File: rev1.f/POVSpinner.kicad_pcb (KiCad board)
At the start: 2 copper layers, 25.3 x 76.4 mm, 26 parts, among them P1 ISP, SW1 SW_RESET, SW2 SW_POWER, U1 Microchip_ATtiny85, X1 USBMICRO

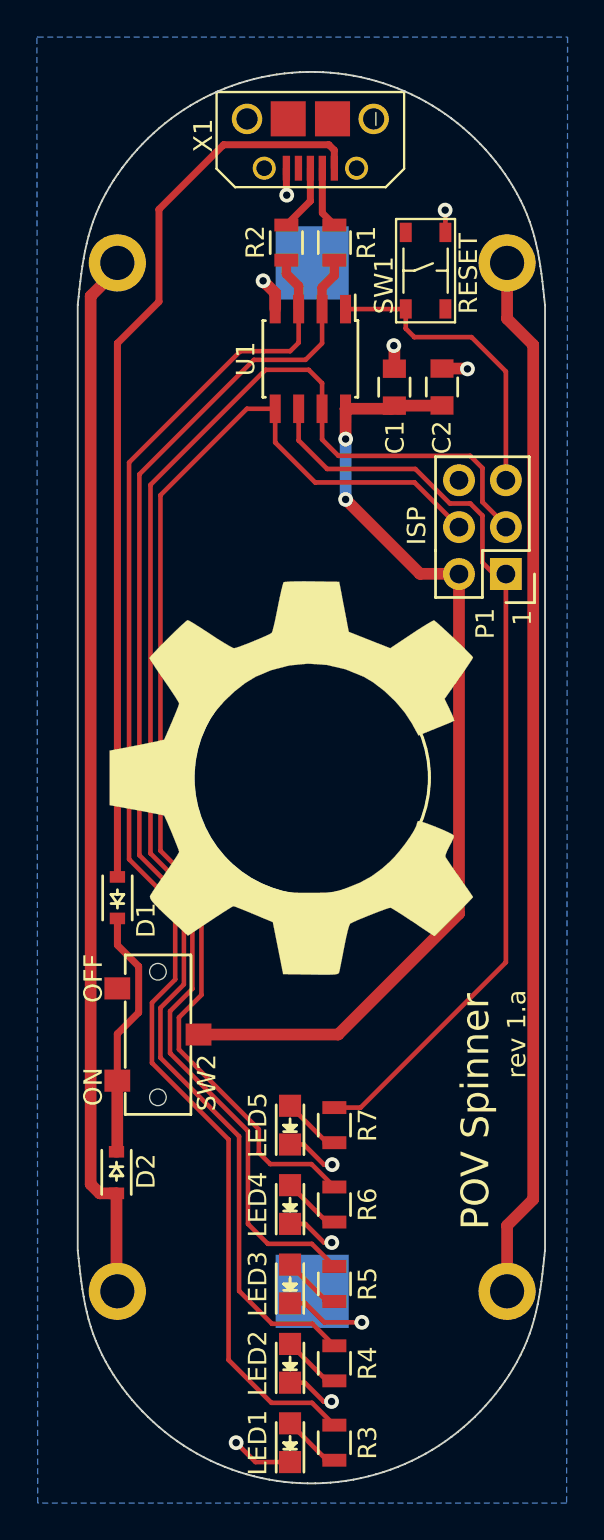
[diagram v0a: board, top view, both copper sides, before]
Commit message: added new 5.3mm soic 8 footprint for AtTiny85
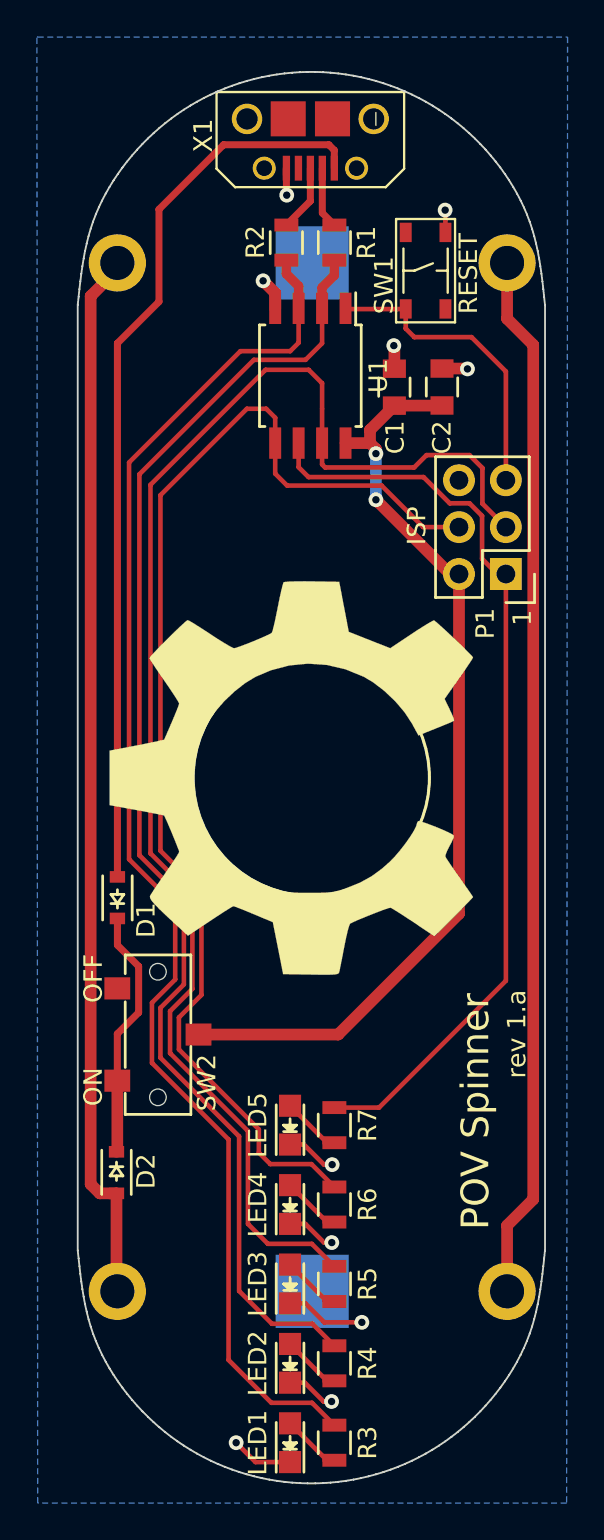
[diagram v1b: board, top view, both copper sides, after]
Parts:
- U1: footprint Housings_SOIC:SOIC-8_3.9x4.9mm_Pitch1.27mm -> Housings_SOIC:SOIJ-8_5.3x5.3mm_Pitch1.27mm
- moved U1 0.91 mm to (124.5, 64.3)
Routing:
- net /+VCC: track 53.6 -> 51.6 mm
- net /PB2: track 77.1 -> 78.4 mm
- net /PB0: track 65.5 -> 66.2 mm
- net /PB1: track 51.0 -> 50.5 mm
